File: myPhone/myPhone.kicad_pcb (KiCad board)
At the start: 2 copper layers, 135 x 70 mm, 211 parts, among them J1 USB_OTG, J2 BATT, J201 ESP32.UART, J202 Modem, J203 SIM_Card, J204 Motor, J205 Micro_SD_Card, J206 Camera, J207 GPS, J3 RV.Debug, J301 iMX8, J4 SJ-3571N, J5 Display, J6 Touch, Q1 MMBT3906, SW1 RESET, SW2 WAKE, SW201 BOOT, U1 BQ25895, U10 74HC595, U11 ICS-43434, U12 MAX98357A, U13 FT813Q, U14 FAN5333BSX, U2 TPS62293, U201 ESP32-WROOM, U202 SN74CBTLV3125, U203 TXB0104RGY, U204 TXB0104RGY, U205 DRV2605L, U206 SN74CBTLV3126, U207 TPS22917, U208 SN74LVC2G66, U209 TPS22917, U3 TPS630250, U4 SN74LVC2G07, U5 E310-G000, U6 IS25LP128-JBLE, U7 74HC00, U8 74HC00, U9 74HC595, X1 SiT1533, Y1 16MHz, Y2 12MHz

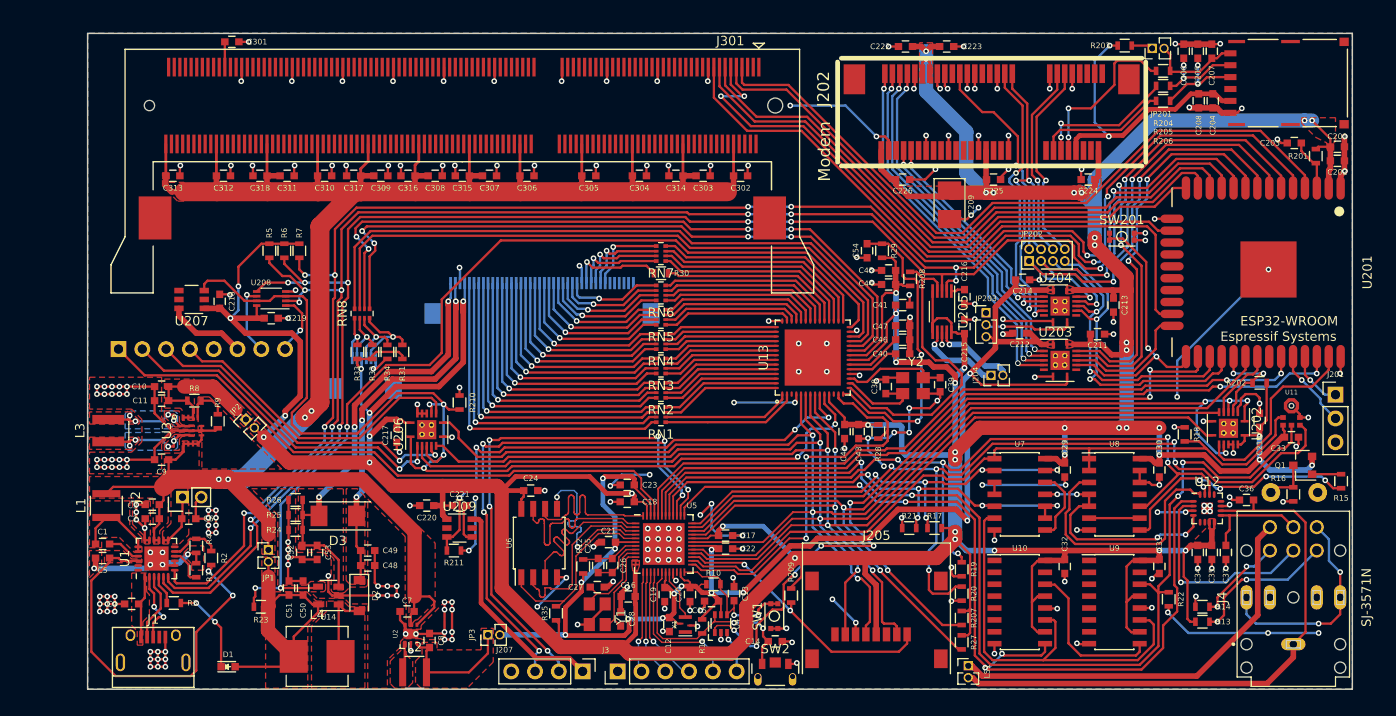
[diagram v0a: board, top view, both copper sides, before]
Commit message: upgrade to kicad 5; fixed footprints
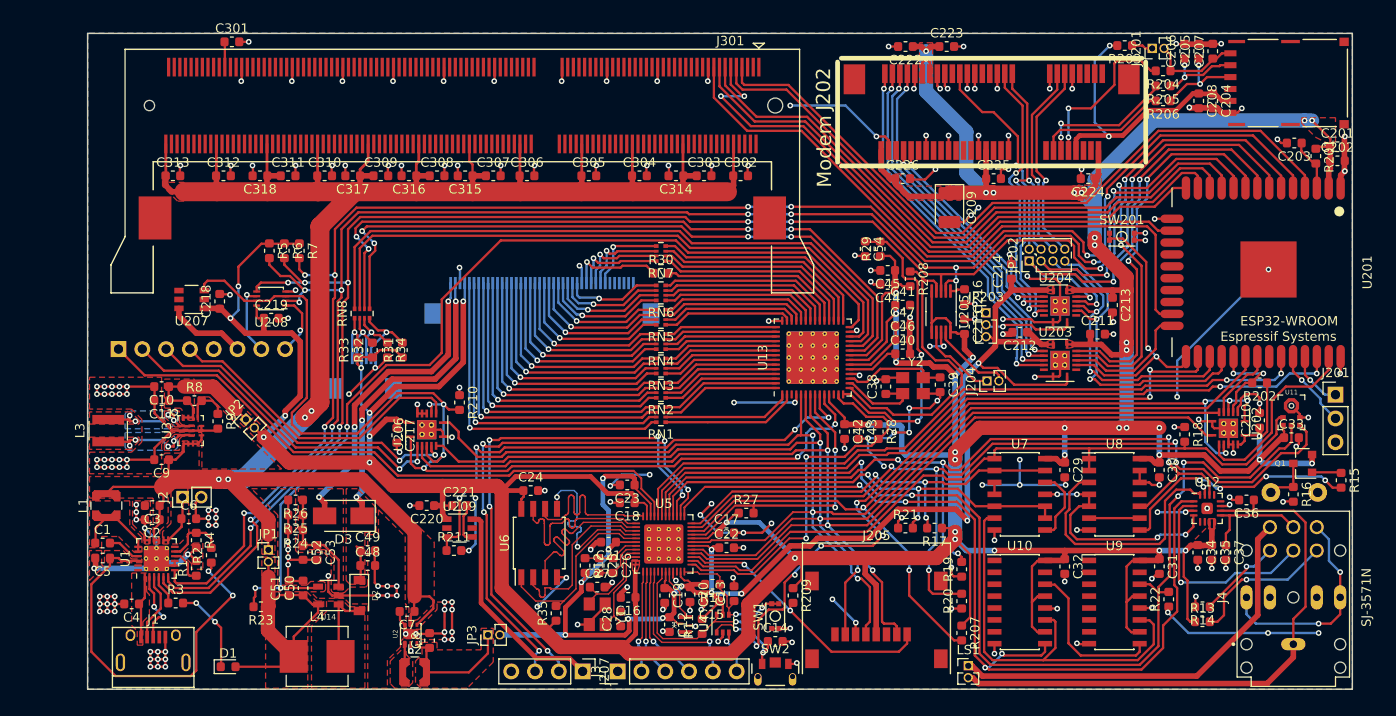
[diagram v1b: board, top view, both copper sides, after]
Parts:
- C1, C10, C11, C12, C13, C14, C15, C16, C17, C18, C19, C2, C20, C201, C202, C203, C204, C205, C206, C207, C208, C21, C210, C211, C212, C213, C214, C215, C216, C217, C218, C219, C22, C220, C221, C222, C223, C224, C225, C226, C23, C24, C25, C26, C27, C28, C29, C3, C30, C301, C302, C303, C304, C305, C306, C307, C308, C309, C31, C310, C311, C312, C313, C314, C315, C316, C317, C318, C32, C33, C34, C35, C36, C37, C38, C39, C4, C40, C41, C42, C43, C44, C45, C46, C47, C48, C49, C5, C50, C51, C52, C53, C54, C6, C7, C8, C9: footprint Capacitors_SMD:C_0603 -> Capacitor_SMD:C_0603_1608Metric
- C209: footprint Capacitors_Tantalum_SMD:CP_Tantalum_Case-B_EIA-3528-21_Reflow -> Capacitor_Tantalum_SMD:CP_EIA-3528-21_Kemet-B
- D1: footprint LEDs:LED_0603 -> LED_SMD:LED_0603_1608Metric
- D2: footprint Diodes_SMD:D_SOD-123 -> Diode_SMD:D_SOD-123
- D3: footprint footprints:DO-214AC -> Diode_SMD:D_SMA
- J2: footprint Pin_Headers:Pin_Header_Straight_1x02_Pitch2.00mm -> Connector_PinHeader_2.00mm:PinHeader_1x02_P2.00mm_Vertical
- J201: footprint Pin_Headers:Pin_Header_Straight_1x03_Pitch2.54mm -> Connector_PinHeader_2.54mm:PinHeader_1x03_P2.54mm_Vertical
- J204, JP1, JP2, JP201, JP3, LS1: footprint Pin_Headers:Pin_Header_Straight_1x02_Pitch1.27mm -> Connector_PinHeader_1.27mm:PinHeader_1x02_P1.27mm_Vertical
- J206: footprint Pin_Headers:Pin_Header_Straight_1x08_Pitch2.54mm -> Connector_PinHeader_2.54mm:PinHeader_1x08_P2.54mm_Vertical
- J207: footprint Pin_Headers:Pin_Header_Straight_1x04_Pitch2.54mm -> Connector_PinHeader_2.54mm:PinHeader_1x04_P2.54mm_Vertical
- J3: footprint Pin_Headers:Pin_Header_Straight_1x06_Pitch2.54mm -> Connector_PinHeader_2.54mm:PinHeader_1x06_P2.54mm_Vertical
- JP202: footprint Pin_Headers:Pin_Header_Straight_2x04_Pitch1.27mm -> Connector_PinHeader_1.27mm:PinHeader_2x04_P1.27mm_Vertical
- JP203: footprint Pin_Headers:Pin_Header_Straight_1x03_Pitch1.27mm -> Connector_PinHeader_1.27mm:PinHeader_1x03_P1.27mm_Vertical
- L1, L2: footprint footprints:Coilcraft_LPS3015 -> footprints:L_Coilcraft_LPS3015
- L3: footprint footprints:Coilcraft_XAL40 -> footprints:L_Coilcraft_XAL40
- L4: footprint footprints:Murata_LQH66SN -> footprints:L_Murata_LQH66SN
- Q1: footprint TO_SOT_Packages_SMD:SOT-23 -> Package_TO_SOT_SMD:SOT-23
- R1, R10, R11, R12, R13, R14, R15, R16, R17, R18, R19, R2, R20, R201, R202, R203, R204, R205, R206, R207, R208, R209, R21, R210, R211, R22, R23, R24, R25, R26, R27, R28, R29, R3, R30, R31, R32, R33, R34, R35, R4, R5, R6, R7, R8, R9: footprint Resistors_SMD:R_0603 -> Resistor_SMD:R_0603_1608Metric
- U1: footprint footprints:QFN-24-1EP_4x4mm_Pitch0.5mm -> Package_DFN_QFN:Texas_S-PWQFN-N24_EP2.7x2.7mm_ThermalVias
- U10, U9: footprint Housings_SOIC:SOIC-16_3.9x9.9mm_Pitch1.27mm -> Package_SO:SOIC-16_3.9x9.9mm_P1.27mm
- U12: footprint footprints:MAX98357 -> Package_DFN_QFN:TQFN-16-1EP_3x3mm_P0.5mm_EP1.23x1.23mm
- U13: footprint footprints:FT813Q -> Package_DFN_QFN:QFN-56-1EP_8x8mm_P0.5mm_EP5.6x5.6mm_ThermalVias
- U14: footprint TO_SOT_Packages_SMD:SOT-23-5 -> Package_TO_SOT_SMD:SOT-23-5
- U202, U203, U204, U206: footprint footprints:Texas_S-PVQFN-N14_ThermalVias -> Package_DFN_QFN:Texas_S-PVQFN-N14_ThermalVias
- U205: footprint footprints:VSSOP-10_3x3mm_Pitch0.5mm -> Package_SO:VSSOP-10_3x3mm_P0.5mm
- U208: footprint Housings_SSOP:VSSOP-8_2.3x2mm_Pitch0.5mm -> Package_SO:VSSOP-8_2.4x2.1mm_P0.5mm
- U4: footprint TO_SOT_Packages_SMD:SC-70-6 -> Package_TO_SOT_SMD:SOT-363_SC-70-6
- U5: footprint Housings_DFN_QFN:UQFN-48-1EP_6x6mm_Pitch0.4mm -> Package_DFN_QFN:QFN-48-1EP_6x6mm_P0.4mm_EP4.2x4.2mm_ThermalVias
- U6: footprint Housings_SOIC:SOIJ-8_5.3x5.3mm_Pitch1.27mm -> Package_SO:SOIJ-8_5.3x5.3mm_P1.27mm
- U7, U8: footprint Housings_SOIC:SOIC-14_3.9x8.7mm_Pitch1.27mm -> Package_SO:SOIC-14_3.9x8.7mm_P1.27mm
- moved R27 26.8 mm to (167.5, 123.0), turned to 0 degrees
- moved R207 1.60 mm to (190.5, 135.8)
- moved C214 1.50 mm to (195.8, 97.2), turned to 90 degrees
- moved R20 0.80 mm to (190.5, 132.4)
- moved J204 0.74 mm to (193.2, 108.9)
- moved D3 0.60 mm to (124.5, 123.3)
- moved R4 0.60 mm to (108.8, 125.9)
- moved C307 0.40 mm to (140.5, 87.0)
- moved R21 0.40 mm to (184.5, 124.6)
- moved C17 0.32 mm to (165.4, 125.1)
- moved C209 0.30 mm to (189.2, 90.4)
- moved C315 0.30 mm to (137.5, 87.0)
- moved R2 0.30 mm to (110.4, 127.5)
- moved C54 0.28 mm to (180.2, 94.8)
- moved R29 0.28 mm to (181.8, 94.8)
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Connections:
- J1 pad 4: Net-(J1-Pad4) -> (no net)
- J202 pad 1: Net-(J202-Pad1) -> (no net)
- J202 pad 16: Net-(J202-Pad16) -> (no net)
- J202 pad 20: Net-(J202-Pad20) -> (no net)
- J202 pad 22: Net-(J202-Pad22) -> (no net)
- J202 pad 23: Net-(J202-Pad23) -> (no net)
- J202 pad 25: Net-(J202-Pad25) -> (no net)
- J202 pad 28: Net-(J202-Pad28) -> (no net)
- J202 pad 3: Net-(J202-Pad3) -> (no net)
- J202 pad 30: Net-(J202-Pad30) -> (no net)
- J202 pad 32: Net-(J202-Pad32) -> (no net)
- J202 pad 33: Net-(J202-Pad33) -> (no net)
- J202 pad 36: Net-(J202-Pad36) -> (no net)
- J202 pad 38: Net-(J202-Pad38) -> (no net)
- J202 pad 42: Net-(J202-Pad42) -> (no net)
- J202 pad 48: Net-(J202-Pad48) -> (no net)
- J202 pad 5: Net-(J202-Pad5) -> (no net)
- J202 pad 6: Net-(J202-Pad6) -> (no net)
- J202 pad 7: Net-(J202-Pad7) -> (no net)
- J203 pad 6: Net-(J203-Pad6) -> (no net)
- J205 pad 3: Net-(J205-Pad3) -> (no net)
- J205 pad 8: Net-(J205-Pad8) -> (no net)
- J301 pad 100: Net-(J301-Pad100) -> (no net)
- J301 pad 101: Net-(J301-Pad101) -> (no net)
- J301 pad 102: Net-(J301-Pad102) -> (no net)
- J301 pad 103: Net-(J301-Pad103) -> (no net)
- J301 pad 104: Net-(J301-Pad104) -> (no net)
- J301 pad 106: Net-(J301-Pad106) -> (no net)
- J301 pad 107: Net-(J301-Pad107) -> (no net)
- J301 pad 108: Net-(J301-Pad108) -> (no net)
- J301 pad 109: Net-(J301-Pad109) -> (no net)
- J301 pad 110: Net-(J301-Pad110) -> (no net)
- J301 pad 111: Net-(J301-Pad111) -> (no net)
- J301 pad 112: Net-(J301-Pad112) -> (no net)
- J301 pad 113: Net-(J301-Pad113) -> (no net)
- J301 pad 115: Net-(J301-Pad115) -> (no net)
- J301 pad 116: Net-(J301-Pad116) -> (no net)
- J301 pad 117: Net-(J301-Pad117) -> (no net)
- J301 pad 118: Net-(J301-Pad118) -> (no net)
- J301 pad 119: Net-(J301-Pad119) -> (no net)
- J301 pad 12: Net-(J301-Pad12) -> (no net)
- J301 pad 120: Net-(J301-Pad120) -> (no net)
- J301 pad 121: Net-(J301-Pad121) -> (no net)
- J301 pad 122: Net-(J301-Pad122) -> (no net)
- J301 pad 124: Net-(J301-Pad124) -> (no net)
- J301 pad 125: Net-(J301-Pad125) -> (no net)
- J301 pad 126: Net-(J301-Pad126) -> (no net)
- J301 pad 127: Net-(J301-Pad127) -> (no net)
- J301 pad 128: Net-(J301-Pad128) -> (no net)
- J301 pad 129: Net-(J301-Pad129) -> (no net)
- J301 pad 130: Net-(J301-Pad130) -> (no net)
- J301 pad 131: Net-(J301-Pad131) -> (no net)
- J301 pad 133: Net-(J301-Pad133) -> (no net)
- J301 pad 134: Net-(J301-Pad134) -> (no net)
- J301 pad 135: Net-(J301-Pad135) -> (no net)
- J301 pad 136: Net-(J301-Pad136) -> (no net)
- J301 pad 137: Net-(J301-Pad137) -> (no net)
- J301 pad 138: Net-(J301-Pad138) -> (no net)
- J301 pad 139: Net-(J301-Pad139) -> (no net)
- J301 pad 14: Net-(J301-Pad14) -> (no net)
- J301 pad 140: Net-(J301-Pad140) -> (no net)
- J301 pad 142: Net-(J301-Pad142) -> (no net)
- J301 pad 143: Net-(J301-Pad143) -> (no net)
- J301 pad 144: Net-(J301-Pad144) -> (no net)
- J301 pad 145: Net-(J301-Pad145) -> (no net)
- J301 pad 146: Net-(J301-Pad146) -> (no net)
- J301 pad 147: Net-(J301-Pad147) -> (no net)
- J301 pad 148: Net-(J301-Pad148) -> (no net)
- J301 pad 149: Net-(J301-Pad149) -> (no net)
- J301 pad 151: Net-(J301-Pad151) -> (no net)
- J301 pad 152: Net-(J301-Pad152) -> (no net)
- J301 pad 153: Net-(J301-Pad153) -> (no net)
- J301 pad 154: Net-(J301-Pad154) -> (no net)
- J301 pad 155: Net-(J301-Pad155) -> (no net)
- J301 pad 156: Net-(J301-Pad156) -> (no net)
- J301 pad 157: Net-(J301-Pad157) -> (no net)
- J301 pad 158: Net-(J301-Pad158) -> (no net)
- J301 pad 16: Net-(J301-Pad16) -> (no net)
- J301 pad 160: Net-(J301-Pad160) -> (no net)
- J301 pad 161: Net-(J301-Pad161) -> (no net)
- J301 pad 162: Net-(J301-Pad162) -> (no net)
- J301 pad 163: Net-(J301-Pad163) -> (no net)
- J301 pad 164: Net-(J301-Pad164) -> (no net)
- J301 pad 165: Net-(J301-Pad165) -> (no net)
- J301 pad 166: Net-(J301-Pad166) -> (no net)
- J301 pad 167: Net-(J301-Pad167) -> (no net)
- J301 pad 169: Net-(J301-Pad169) -> (no net)
- J301 pad 170: Net-(J301-Pad170) -> (no net)
- J301 pad 171: Net-(J301-Pad171) -> (no net)
- J301 pad 172: Net-(J301-Pad172) -> (no net)
- J301 pad 173: Net-(J301-Pad173) -> (no net)
- J301 pad 174: Net-(J301-Pad174) -> (no net)
- J301 pad 175: Net-(J301-Pad175) -> (no net)
- J301 pad 176: Net-(J301-Pad176) -> (no net)
- J301 pad 178: Net-(J301-Pad178) -> (no net)
- J301 pad 179: Net-(J301-Pad179) -> (no net)
- J301 pad 18: Net-(J301-Pad18) -> (no net)
- J301 pad 180: Net-(J301-Pad180) -> (no net)
- J301 pad 181: Net-(J301-Pad181) -> (no net)
- J301 pad 182: Net-(J301-Pad182) -> (no net)
- J301 pad 184: Net-(J301-Pad184) -> (no net)
- J301 pad 185: Net-(J301-Pad185) -> (no net)
- J301 pad 187: Net-(J301-Pad187) -> (no net)
- J301 pad 188: Net-(J301-Pad188) -> (no net)
- J301 pad 189: Net-(J301-Pad189) -> (no net)
- J301 pad 190: Net-(J301-Pad190) -> (no net)
- J301 pad 191: Net-(J301-Pad191) -> (no net)
- J301 pad 192: Net-(J301-Pad192) -> (no net)
- J301 pad 193: Net-(J301-Pad193) -> (no net)
- J301 pad 194: Net-(J301-Pad194) -> (no net)
- J301 pad 195: Net-(J301-Pad195) -> (no net)
- J301 pad 196: Net-(J301-Pad196) -> (no net)
- J301 pad 197: Net-(J301-Pad197) -> (no net)
- J301 pad 198: Net-(J301-Pad198) -> (no net)
- J301 pad 199: Net-(J301-Pad199) -> (no net)
- J301 pad 2: Net-(J301-Pad2) -> (no net)
- J301 pad 20: Net-(J301-Pad20) -> (no net)
- J301 pad 200: Net-(J301-Pad200) -> (no net)
- J301 pad 201: Net-(J301-Pad201) -> (no net)
- J301 pad 202: Net-(J301-Pad202) -> (no net)
- J301 pad 203: Net-(J301-Pad203) -> (no net)
- J301 pad 21: Net-(J301-Pad21) -> (no net)
- J301 pad 22: Net-(J301-Pad22) -> (no net)
- J301 pad 23: Net-(J301-Pad23) -> (no net)
- J301 pad 24: Net-(J301-Pad24) -> (no net)
- J301 pad 25: Net-(J301-Pad25) -> (no net)
- J301 pad 26: Net-(J301-Pad26) -> (no net)
- J301 pad 27: Net-(J301-Pad27) -> (no net)
- J301 pad 29: Net-(J301-Pad29) -> (no net)
- J301 pad 3: Net-(J301-Pad3) -> (no net)
- J301 pad 30: Net-(J301-Pad30) -> (no net)
- J301 pad 31: Net-(J301-Pad31) -> (no net)
- J301 pad 32: Net-(J301-Pad32) -> (no net)
- J301 pad 33: Net-(J301-Pad33) -> (no net)
- J301 pad 34: Net-(J301-Pad34) -> (no net)
- J301 pad 35: Net-(J301-Pad35) -> (no net)
- J301 pad 36: Net-(J301-Pad36) -> (no net)
- J301 pad 38: Net-(J301-Pad38) -> (no net)
- J301 pad 39: Net-(J301-Pad39) -> (no net)
- J301 pad 4: Net-(J301-Pad4) -> (no net)
- J301 pad 40: Net-(J301-Pad40) -> (no net)
- J301 pad 41: Net-(J301-Pad41) -> (no net)
- J301 pad 42: Net-(J301-Pad42) -> (no net)
- J301 pad 43: Net-(J301-Pad43) -> (no net)
- J301 pad 44: Net-(J301-Pad44) -> (no net)
- J301 pad 45: Net-(J301-Pad45) -> (no net)
- J301 pad 47: Net-(J301-Pad47) -> (no net)
- J301 pad 48: Net-(J301-Pad48) -> (no net)
- J301 pad 49: Net-(J301-Pad49) -> (no net)
- J301 pad 5: Net-(J301-Pad5) -> (no net)
- J301 pad 50: Net-(J301-Pad50) -> (no net)
- J301 pad 51: Net-(J301-Pad51) -> (no net)
- J301 pad 52: Net-(J301-Pad52) -> (no net)
- J301 pad 53: Net-(J301-Pad53) -> (no net)
- J301 pad 54: Net-(J301-Pad54) -> (no net)
- J301 pad 56: Net-(J301-Pad56) -> (no net)
- J301 pad 57: Net-(J301-Pad57) -> (no net)
- J301 pad 58: Net-(J301-Pad58) -> (no net)
- J301 pad 59: Net-(J301-Pad59) -> (no net)
- J301 pad 6: Net-(J301-Pad6) -> (no net)
- J301 pad 60: Net-(J301-Pad60) -> (no net)
- J301 pad 61: Net-(J301-Pad61) -> (no net)
- J301 pad 62: Net-(J301-Pad62) -> (no net)
- J301 pad 63: Net-(J301-Pad63) -> (no net)
- J301 pad 65: Net-(J301-Pad65) -> (no net)
- J301 pad 66: Net-(J301-Pad66) -> (no net)
- J301 pad 67: Net-(J301-Pad67) -> (no net)
- J301 pad 68: Net-(J301-Pad68) -> (no net)
- J301 pad 69: Net-(J301-Pad69) -> (no net)
- J301 pad 70: Net-(J301-Pad70) -> (no net)
- J301 pad 72: Net-(J301-Pad72) -> (no net)
- J301 pad 73: Net-(J301-Pad73) -> (no net)
- J301 pad 74: Net-(J301-Pad74) -> (no net)
- J301 pad 75: Net-(J301-Pad75) -> (no net)
- J301 pad 76: Net-(J301-Pad76) -> (no net)
- J301 pad 77: Net-(J301-Pad77) -> (no net)
- J301 pad 79: Net-(J301-Pad79) -> (no net)
- J301 pad 8: Net-(J301-Pad8) -> (no net)
- J301 pad 80: Net-(J301-Pad80) -> (no net)
- J301 pad 81: Net-(J301-Pad81) -> (no net)
- J301 pad 82: Net-(J301-Pad82) -> (no net)
- J301 pad 83: Net-(J301-Pad83) -> (no net)
- J301 pad 84: Net-(J301-Pad84) -> (no net)
- J301 pad 85: Net-(J301-Pad85) -> (no net)
- J301 pad 86: Net-(J301-Pad86) -> (no net)
- J301 pad 88: Net-(J301-Pad88) -> (no net)
- J301 pad 89: Net-(J301-Pad89) -> (no net)
- J301 pad 90: Net-(J301-Pad90) -> (no net)
- J301 pad 91: Net-(J301-Pad91) -> (no net)
- J301 pad 92: Net-(J301-Pad92) -> (no net)
- J301 pad 93: Net-(J301-Pad93) -> (no net)
- J301 pad 94: Net-(J301-Pad94) -> (no net)
- J301 pad 95: Net-(J301-Pad95) -> (no net)
- J301 pad 97: Net-(J301-Pad97) -> (no net)
- J301 pad 98: Net-(J301-Pad98) -> (no net)
- J301 pad 99: Net-(J301-Pad99) -> (no net)
- J4 pad 10: Net-(J4-Pad10) -> (no net)
- J4 pad 11: Net-(J4-Pad11) -> (no net)
- J5 pad 35: Net-(J5-Pad35) -> (no net)
- J5 pad 37: Net-(J5-Pad37) -> (no net)
- J5 pad 38: Net-(J5-Pad38) -> (no net)
- J5 pad 39: Net-(J5-Pad39) -> (no net)
- J5 pad 40: Net-(J5-Pad40) -> (no net)
- U1 pad 12: Net-(U1-Pad12) -> (no net)
- U1 pad 23: Net-(U1-Pad23) -> (no net)
- U1 pad 24: Net-(U1-Pad24) -> (no net)
- U10 pad 1: Net-(U10-Pad1) -> (no net)
- U10 pad 15: Net-(U10-Pad15) -> (no net)
- U10 pad 2: Net-(U10-Pad2) -> (no net)
- U10 pad 3: Net-(U10-Pad3) -> (no net)
- U10 pad 4: Net-(U10-Pad4) -> (no net)
- U10 pad 5: Net-(U10-Pad5) -> (no net)
- U10 pad 6: Net-(U10-Pad6) -> (no net)
- U10 pad 7: Net-(U10-Pad7) -> (no net)
- U13 pad 12: Net-(U13-Pad12) -> (no net)
- U13 pad 3: Net-(U13-Pad3) -> (no net)
- U201 pad 17: Net-(U201-Pad17) -> (no net)
- U201 pad 18: Net-(U201-Pad18) -> (no net)
- U201 pad 19: Net-(U201-Pad19) -> (no net)
- U201 pad 20: Net-(U201-Pad20) -> (no net)
- U201 pad 21: Net-(U201-Pad21) -> (no net)
- U201 pad 22: Net-(U201-Pad22) -> (no net)
- U201 pad 32: Net-(U201-Pad32) -> (no net)
- U203 pad 6: Net-(U203-Pad6) -> (no net)
- U203 pad 9: Net-(U203-Pad9) -> (no net)
- U204 pad 6: Net-(U204-Pad6) -> (no net)
- U204 pad 9: Net-(U204-Pad9) -> (no net)
- U207 pad 4: Net-(U207-Pad4) -> (no net)
- U207 pad 5: Net-(U207-Pad5) -> (no net)
- U209 pad 5: Net-(U209-Pad5) -> (no net)
- U5 pad 17: Net-(U5-Pad17) -> (no net)
- U5 pad 22: Net-(U5-Pad22) -> (no net)
- U8 pad 11: Net-(U8-Pad11) -> (no net)
- U9 pad 1: Net-(U9-Pad1) -> (no net)
- U9 pad 15: Net-(U9-Pad15) -> (no net)
- U9 pad 2: Net-(U9-Pad2) -> (no net)
- U9 pad 3: Net-(U9-Pad3) -> (no net)
- U9 pad 4: Net-(U9-Pad4) -> (no net)
- U9 pad 5: Net-(U9-Pad5) -> (no net)
- U9 pad 6: Net-(U9-Pad6) -> (no net)
- U9 pad 7: Net-(U9-Pad7) -> (no net)
- X1 pad 1: Net-(X1-Pad1) -> (no net)
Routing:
- net GND: track 458.6 -> 489.1 mm, vias 264 -> 240
- net SPI1.SS2: track 50.7 -> 30.6 mm, vias 3 -> 2
- net +3V3: track 674.0 -> 668.5 mm, vias 46 -> 45
- net PWM2.2: track 50.1 -> 46.1 mm, vias 5 -> 3
- net /DISP_LED_A: track 39.9 -> 36.1 mm
- net GPIO_18: track 53.8 -> 50.0 mm, vias 5 -> 3
- net GPIO_0: track 42.4 -> 40.4 mm
- net PWM0.1: track 78.4 -> 76.5 mm
- net /DISP_LED_K: track 47.9 -> 46.0 mm
- net +1V8: track 180.3 -> 179.0 mm
- net Net-(C13-Pad1): track 16.4 -> 15.3 mm
- net Net-(R2-Pad2): track 5.50 -> 6.58 mm
- net FT813.GPIO3: track 33.7 -> 32.6 mm
- net Net-(J6-Pad5): track 8.99 -> 8.25 mm
- net SPI1.SS3: track 97.1 -> 96.4 mm
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
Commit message: REV1 board
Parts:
- removed C15: 0.1uF, Capacitor_SMD:C_0603_1608Metric
- removed C209: 470uF, Capacitor_Tantalum_SMD:CP_EIA-3528-21_Kemet-B
- removed J201: ESP32.UART, Connector_PinHeader_2.54mm:PinHeader_1x03_P2.54mm_Vertical
- removed J207: GPS, Connector_PinHeader_2.54mm:PinHeader_1x04_P2.54mm_Vertical
- removed J4: SJ-3571N, footprints:CUI_SJ-3571N
- removed J5: Display, footprints:Hirose_FH12-40S-0.5SH_1x40-1MP_P0.50mm_Horizontal_Bottom
- removed J6: Touch, footprints:Hirose_FH12-6S-0.5SH_1x06-1MP_P0.50mm_Horizontal_Bottom
- removed the JP202 at (197.7, 96.1)
- removed R30: 33R, Resistor_SMD:R_0603_1608Metric
- removed RN1, RN2, RN3, RN4, RN5, RN6, RN7, RN8: 33R, footprints:R_Array_Convex_4x0402
- removed U4: SN74LVC2G07, Package_TO_SOT_SMD:SOT-363_SC-70-6
- added C227: 470uF, Capacitor_Tantalum_SMD:CP_EIA-3528-21_Kemet-B, F.Cu at (190.1, 73.5)
- added C228: 470uF, Capacitor_Tantalum_SMD:CP_EIA-3528-21_Kemet-B, F.Cu at (183.3, 73.5)
- added C319: 1uF, Capacitor_SMD:C_0603_1608Metric, F.Cu at (127.6, 89.8)
- added C320: 0.1uF, Capacitor_SMD:C_0603_1608Metric, F.Cu at (129.1, 89.8)
- added C321: 1uF, Capacitor_SMD:C_0603_1608Metric, F.Cu at (127.6, 100.2)
- added C322: 0.1uF, Capacitor_SMD:C_0603_1608Metric, F.Cu at (129.1, 100.2)
- added C323: 0.1uF, Capacitor_SMD:C_0603_1608Metric, B.Cu at (147.9, 90.7)
- added C324: 0.01uF, Capacitor_SMD:C_0603_1608Metric, B.Cu at (147.9, 89.2)
- added C325: 1uF, Capacitor_SMD:C_0603_1608Metric, F.Cu at (137.9, 111.2)
- added C326: 0.1uF, Capacitor_SMD:C_0603_1608Metric, F.Cu at (137.9, 109.8)
- added C327: 1uF, Capacitor_SMD:C_0603_1608Metric, F.Cu at (148.3, 111.2)
- added C328: 0.1uF, Capacitor_SMD:C_0603_1608Metric, F.Cu at (148.3, 109.8)
- added C329: 0.1uF, Capacitor_SMD:C_0603_1608Metric, B.Cu at (139.8, 94.5)
- added C330: 0.01uF, Capacitor_SMD:C_0603_1608Metric, B.Cu at (139.8, 93.0)
- added C331: 0.1uF, Capacitor_SMD:C_0603_1608Metric, B.Cu at (142.7, 95.0)
- added C332: 0.01uF, Capacitor_SMD:C_0603_1608Metric, B.Cu at (144.7, 95.0)
- added C333: 0.1uF, Capacitor_SMD:C_0603_1608Metric, B.Cu at (147.9, 94.2)
- added C334: 0.01uF, Capacitor_SMD:C_0603_1608Metric, B.Cu at (147.9, 92.7)
- added C335: 0.1uF, Capacitor_SMD:C_0603_1608Metric, B.Cu at (139.8, 88.8)
- added C336: 0.01uF, Capacitor_SMD:C_0603_1608Metric, B.Cu at (139.8, 90.2)
- added C337: 1uF, Capacitor_SMD:C_0603_1608Metric, F.Cu at (151.3, 111.2)
- added C338: 0.1uF, Capacitor_SMD:C_0603_1608Metric, F.Cu at (151.3, 109.8)
- added C339: 1uF, Capacitor_SMD:C_0603_1608Metric, F.Cu at (161.7, 111.2)
- added C340: 0.1uF, Capacitor_SMD:C_0603_1608Metric, F.Cu at (161.7, 109.8)
- added C341: 0.1uF, Capacitor_SMD:C_0603_1608Metric, F.Cu at (127.2, 107.2)
- added C342: 0.1uF, Capacitor_SMD:C_0603_1608Metric, F.Cu at (136.7, 115.2)
- added J302: Touch, Connector_FFC-FPC:Hirose_FH12-6S-0.5SH_1x06-1MP_P0.50mm_Horizontal, B.Cu at (126.7, 105.3)
- added J303: Display, Connector_FFC-FPC:Hirose_FH12-40S-0.5SH_1x40-1MP_P0.50mm_Horizontal, B.Cu at (145.7, 113.3)
- added J304: Prog, Connector_FFC-FPC:Hirose_FH12-12S-0.5SH_1x12-1MP_P0.50mm_Horizontal, B.Cu at (141.3, 136.9)
- added JP203: Q.DTR, Connector_PinHeader_1.27mm:PinHeader_1x02_P1.27mm_Vertical, F.Cu at (195.1, 73.4)
- added JP204: Q.RI, Connector_PinHeader_1.27mm:PinHeader_1x02_P1.27mm_Vertical, F.Cu at (198.7, 73.4)
- added JP205: Q.TXD, Connector_PinHeader_1.27mm:PinHeader_1x02_P1.27mm_Vertical, F.Cu at (202.2, 73.4)
- added JP206: Q.RXD, Connector_PinHeader_1.27mm:PinHeader_1x02_P1.27mm_Vertical, F.Cu at (205.8, 73.4)
- added R36: 100K, Resistor_SMD:R_0603_1608Metric, F.Cu at (138.0, 133.3)
- added U301: SN65LVDS822_SWAP, Package_DFN_QFN:QFN-48-1EP_7x7mm_P0.5mm_EP5.15x5.15mm_ThermalVias, F.Cu at (143.8, 90.9)
- added U302: TS3DDR3812, footprints:Texas_R-PWQFN-N42, F.Cu at (132.8, 95.0)
- added U303: TS3DDR3812, footprints:Texas_R-PWQFN-N42, F.Cu at (143.1, 106.0)
- added U304: TS3DDR3812, footprints:Texas_R-PWQFN-N42, F.Cu at (156.5, 106.0)
- C222, C223, C224, C225, C226, C301, C302, C303, C304, C305, C306, C307, C308, C309, C310, C311, C312, C313, C314, C315, C316, C317, C318, J203, J205: moved to B.Cu
- J3: value RV.Debug -> SJ-3571N; footprint Connector_PinHeader_2.54mm:PinHeader_1x06_P2.54mm_Vertical -> footprints:CUI_SJ-3571N
- R208: value 47K -> 100K
- U10, U9: footprint Package_SO:SOIC-16_3.9x9.9mm_P1.27mm -> footprints:74HC595BQ115
- U12: footprint Package_DFN_QFN:TQFN-16-1EP_3x3mm_P0.5mm_EP1.23x1.23mm -> footprints:TQFN-16-1EP_3x3mm_P0.5mm_EP1.23x1.23mm_ThermalVias
- U5: value E310-G000 -> E310-G002
- U7, U8: footprint Package_SO:SOIC-14_3.9x8.7mm_P1.27mm -> footprints:74HC00BQ115
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- renumbered C20 to C19, C22 to C20, C23 to C21, C19 to C22, C21 to C23, JP203 to JP202, R31 to R301, R32 to R302, R33 to R303, R34 to R304
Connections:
- net /DISP_LED_A renamed DISP_LED_A
- net /DISP_LED_K renamed DISP_LED_K
- net Net-(C25-Pad2) renamed /PLL_AVSS
- net Net-(C27-Pad1) renamed /XTAL_XI
- net Net-(C28-Pad1) renamed /XTAL_XO
- net Net-(R35-Pad2) renamed /QSPI_CS
- net Net-(U5-Pad1) renamed /QSPI_DQ_3
- net Net-(U5-Pad2) renamed /QSPI_DQ_2
- net Net-(U5-Pad20) renamed /PSD_LFALTCLK
- net Net-(U5-Pad3) renamed /QSPI_DQ_1
- net Net-(U5-Pad4) renamed /QSPI_DQ_0
- net Net-(U5-Pad48) renamed /QSPI_CLK
- C12 pad 1: +1V8 -> +3V3
- C13 pad 1: Net-(C13-Pad1) -> RESET
- C14 pad 1: Net-(C14-Pad1) -> WAKE
- C19 pad 1: +1V8 -> +3V3
- C23 pad 1: +1V8 -> +3V3
- C25 pad 1: Net-(C25-Pad1) -> /PLL_AVDD
- C26 pad 1: Net-(C25-Pad1) -> /PLL_AVDD
- J1 pad 4: (no net) -> Net-(J1-Pad4)
- J202 pad 1: (no net) -> Net-(J202-Pad1)
- J202 pad 16: (no net) -> Net-(J202-Pad16)
- J202 pad 20: (no net) -> Net-(J202-Pad20)
- J202 pad 22: (no net) -> Net-(J202-Pad22)
- J202 pad 23: (no net) -> Net-(J202-Pad23)
- J202 pad 25: (no net) -> Net-(J202-Pad25)
- J202 pad 28: (no net) -> Net-(J202-Pad28)
- J202 pad 3: (no net) -> Net-(J202-Pad3)
- J202 pad 30: (no net) -> Net-(J202-Pad30)
- J202 pad 32: (no net) -> Net-(J202-Pad32)
- J202 pad 33: (no net) -> Net-(J202-Pad33)
- J202 pad 36: (no net) -> iMX8_USB1_D_N
- J202 pad 38: (no net) -> iMX8_USB1_D_P
- J202 pad 42: (no net) -> Net-(J202-Pad42)
- J202 pad 48: (no net) -> Net-(J202-Pad48)
- J202 pad 5: (no net) -> Net-(J202-Pad5)
- J202 pad 6: (no net) -> Net-(J202-Pad6)
- J202 pad 7: (no net) -> Net-(J202-Pad7)
- J203 pad 6: (no net) -> Net-(J203-Pad6)
- J205 pad 3: (no net) -> Net-(J205-Pad3)
- J205 pad 8: (no net) -> Net-(J205-Pad8)
- J3 pad 1: GND -> /SPK_VO-
- J3 pad 2: JTAG_TCK -> Net-(J3-Pad2)
- J3 pad 3: JTAG_TDO -> Net-(J3-Pad2)
- J3 pad 4: JTAG_TMS -> Net-(J3-Pad4)
- J3 pad 5: JTAG_TDI -> /SPK_GAIN
- J3 pad 6: RESET -> Net-(J3-Pad6)
- J301 pad 100: (no net) -> Net-(J301-Pad100)
- J301 pad 101: (no net) -> Net-(J301-Pad101)
- J301 pad 102: (no net) -> Net-(J301-Pad102)
- J301 pad 103: (no net) -> Net-(J301-Pad103)
- J301 pad 104: (no net) -> Net-(J301-Pad104)
- J301 pad 106: (no net) -> Net-(J301-Pad106)
- J301 pad 107: (no net) -> Net-(J301-Pad107)
- J301 pad 108: (no net) -> Net-(J301-Pad108)
- J301 pad 109: (no net) -> Net-(J301-Pad109)
- J301 pad 110: (no net) -> Net-(J301-Pad110)
- J301 pad 111: (no net) -> Net-(J301-Pad111)
- J301 pad 112: (no net) -> Net-(J301-Pad112)
- J301 pad 113: (no net) -> Net-(J301-Pad113)
- J301 pad 115: (no net) -> Net-(J301-Pad115)
- J301 pad 116: (no net) -> Net-(J301-Pad116)
- J301 pad 117: (no net) -> Net-(J301-Pad117)
- J301 pad 118: (no net) -> Net-(J301-Pad118)
- J301 pad 119: (no net) -> Net-(J301-Pad119)
- J301 pad 12: (no net) -> Net-(J301-Pad12)
- J301 pad 120: (no net) -> Net-(J301-Pad120)
- J301 pad 121: (no net) -> Net-(J301-Pad121)
- J301 pad 122: (no net) -> Net-(J301-Pad122)
- J301 pad 124: (no net) -> Net-(J301-Pad124)
- J301 pad 125: (no net) -> Net-(J301-Pad125)
- J301 pad 126: (no net) -> Net-(J301-Pad126)
- J301 pad 127: (no net) -> Net-(J301-Pad127)
- J301 pad 128: (no net) -> Net-(J301-Pad128)
- J301 pad 129: (no net) -> iMX8_I2C1_SCL
- J301 pad 130: (no net) -> Net-(J301-Pad130)
- J301 pad 131: (no net) -> Net-(J301-Pad131)
- J301 pad 133: (no net) -> Net-(J301-Pad133)
- J301 pad 134: (no net) -> Net-(J301-Pad134)
- J301 pad 135: (no net) -> iMX8_I2C1_SDA
- J301 pad 136: (no net) -> Net-(J301-Pad136)
- J301 pad 137: (no net) -> Net-(J301-Pad137)
- J301 pad 138: (no net) -> Net-(J301-Pad138)
- J301 pad 139: (no net) -> Net-(J301-Pad139)
- J301 pad 14: (no net) -> Net-(J301-Pad14)
- J301 pad 140: (no net) -> Net-(J301-Pad140)
- J301 pad 142: (no net) -> Net-(J301-Pad142)
- J301 pad 143: (no net) -> Net-(J301-Pad143)
- J301 pad 144: (no net) -> Net-(J301-Pad144)
- J301 pad 145: (no net) -> Net-(J301-Pad145)
- J301 pad 146: (no net) -> Net-(J301-Pad146)
- J301 pad 147: (no net) -> Net-(J301-Pad147)
- J301 pad 148: (no net) -> Net-(J301-Pad148)
- J301 pad 149: (no net) -> iMX8_GPIO3_IO13
- J301 pad 151: (no net) -> iMX8_GPIO3_IO12
- J301 pad 152: (no net) -> Net-(J301-Pad152)
- J301 pad 153: (no net) -> iMX8_GPIO3_IO11
- J301 pad 154: (no net) -> Net-(J301-Pad154)
- J301 pad 155: (no net) -> Net-(J301-Pad155)
- J301 pad 156: (no net) -> Net-(J301-Pad156)
- J301 pad 157: (no net) -> Net-(J301-Pad157)
- J301 pad 158: (no net) -> Net-(J301-Pad158)
- J301 pad 16: (no net) -> Net-(J301-Pad16)
- J301 pad 160: (no net) -> Net-(J301-Pad160)
- J301 pad 161: (no net) -> Net-(J301-Pad161)
- J301 pad 162: (no net) -> Net-(J301-Pad162)
- J301 pad 163: (no net) -> Net-(J301-Pad163)
- J301 pad 164: (no net) -> Net-(J301-Pad164)
- J301 pad 165: (no net) -> Net-(J301-Pad165)
- J301 pad 166: (no net) -> Net-(J301-Pad166)
- J301 pad 167: (no net) -> Net-(J301-Pad167)
- J301 pad 169: (no net) -> Net-(J301-Pad169)
- J301 pad 170: (no net) -> Net-(J301-Pad170)
- J301 pad 171: (no net) -> Net-(J301-Pad171)
- J301 pad 172: (no net) -> Net-(J301-Pad172)
- J301 pad 173: (no net) -> Net-(J301-Pad173)
- J301 pad 174: (no net) -> Net-(J301-Pad174)
- J301 pad 175: (no net) -> Net-(J301-Pad175)
- J301 pad 176: (no net) -> iMX8_USB1_D_P
- J301 pad 178: (no net) -> iMX8_USB1_D_N
- J301 pad 179: (no net) -> Net-(J301-Pad179)
- J301 pad 18: (no net) -> Net-(J301-Pad18)
- J301 pad 180: (no net) -> Net-(J301-Pad180)
- J301 pad 181: (no net) -> Net-(J301-Pad181)
- J301 pad 182: (no net) -> Net-(J301-Pad182)
- J301 pad 184: (no net) -> Net-(J301-Pad184)
- J301 pad 185: (no net) -> Net-(J301-Pad185)
- J301 pad 187: (no net) -> Net-(J301-Pad187)
- J301 pad 188: (no net) -> Net-(J301-Pad188)
- J301 pad 189: (no net) -> Net-(J301-Pad189)
- J301 pad 190: (no net) -> Net-(J301-Pad190)
- J301 pad 191: (no net) -> Net-(J301-Pad191)
- J301 pad 192: (no net) -> Net-(J301-Pad192)
- J301 pad 193: (no net) -> Net-(J301-Pad193)
- J301 pad 194: (no net) -> Net-(J301-Pad194)
- J301 pad 195: (no net) -> Net-(J301-Pad195)
- J301 pad 196: (no net) -> Net-(J301-Pad196)
- J301 pad 197: (no net) -> Net-(J301-Pad197)
- J301 pad 198: (no net) -> Net-(J301-Pad198)
- J301 pad 199: (no net) -> Net-(J301-Pad199)
- J301 pad 2: (no net) -> Net-(J301-Pad2)
- J301 pad 20: (no net) -> Net-(J301-Pad20)
- J301 pad 200: (no net) -> Net-(J301-Pad200)
- J301 pad 201: (no net) -> Net-(J301-Pad201)
- J301 pad 202: (no net) -> Net-(J301-Pad202)
- J301 pad 203: (no net) -> Net-(J301-Pad203)
- J301 pad 21: (no net) -> Net-(J301-Pad21)
- J301 pad 22: (no net) -> Net-(J301-Pad22)
- J301 pad 23: (no net) -> Net-(J301-Pad23)
- J301 pad 24: (no net) -> Net-(J301-Pad24)
- J301 pad 25: (no net) -> Net-(J301-Pad25)
- J301 pad 26: (no net) -> Net-(J301-Pad26)
- J301 pad 27: (no net) -> Net-(J301-Pad27)
- J301 pad 29: (no net) -> Net-(J301-Pad29)
- J301 pad 3: (no net) -> Net-(J301-Pad3)
- J301 pad 30: (no net) -> Net-(J301-Pad30)
- J301 pad 31: (no net) -> Net-(J301-Pad31)
- J301 pad 32: (no net) -> Net-(J301-Pad32)
- J301 pad 33: (no net) -> iMX8_LVDS0_CLK_P
- J301 pad 34: (no net) -> Net-(J301-Pad34)
- J301 pad 35: (no net) -> iMX8_LVDS0_CLK_N
- J301 pad 36: (no net) -> Net-(J301-Pad36)
- J301 pad 38: (no net) -> Net-(J301-Pad38)
- J301 pad 39: (no net) -> iMX8_LVDS0_A0_P
- J301 pad 4: (no net) -> Net-(J301-Pad4)
- J301 pad 40: (no net) -> Net-(J301-Pad40)
- J301 pad 41: (no net) -> iMX8_LVDS0_A0_N
- J301 pad 42: (no net) -> Net-(J301-Pad42)
- J301 pad 43: (no net) -> Net-(J301-Pad43)
- J301 pad 44: (no net) -> Net-(J301-Pad44)
- J301 pad 45: (no net) -> iMX8_LVDS0_A1_P
- J301 pad 47: (no net) -> iMX8_LVDS0_A1_N
- J301 pad 48: (no net) -> Net-(J301-Pad48)
- J301 pad 49: (no net) -> Net-(J301-Pad49)
- J301 pad 5: (no net) -> iMX8_GPIO5_IO28
- J301 pad 50: (no net) -> Net-(J301-Pad50)
- J301 pad 51: (no net) -> iMX8_LVDS0_A2_P
- J301 pad 52: (no net) -> Net-(J301-Pad52)
- J301 pad 53: (no net) -> iMX8_LVDS0_A2_N
- J301 pad 54: (no net) -> Net-(J301-Pad54)
- J301 pad 56: (no net) -> Net-(J301-Pad56)
- J301 pad 57: (no net) -> iMX8_LVDS0_A3_P
- J301 pad 58: (no net) -> iMX8_GPIO5_IO25
- J301 pad 59: (no net) -> iMX8_LVDS0_A3_N
- J301 pad 6: (no net) -> Net-(J301-Pad6)
- J301 pad 60: (no net) -> Net-(J301-Pad60)
- J301 pad 61: (no net) -> Net-(J301-Pad61)
- J301 pad 62: (no net) -> Net-(J301-Pad62)
- J301 pad 63: (no net) -> Net-(J301-Pad63)
- J301 pad 65: (no net) -> Net-(J301-Pad65)
- J301 pad 66: (no net) -> Net-(J301-Pad66)
- J301 pad 67: (no net) -> Net-(J301-Pad67)
- J301 pad 68: (no net) -> Net-(J301-Pad68)
- J301 pad 69: (no net) -> Net-(J301-Pad69)
- J301 pad 70: (no net) -> Net-(J301-Pad70)
- J301 pad 72: (no net) -> Net-(J301-Pad72)
- J301 pad 73: (no net) -> Net-(J301-Pad73)
- J301 pad 74: (no net) -> Net-(J301-Pad74)
- J301 pad 75: (no net) -> iMX8_PWM1
- J301 pad 76: (no net) -> Net-(J301-Pad76)
- J301 pad 77: (no net) -> Net-(J301-Pad77)
- J301 pad 79: (no net) -> Net-(J301-Pad79)
- J301 pad 8: (no net) -> Net-(J301-Pad8)
- J301 pad 80: (no net) -> Net-(J301-Pad80)
- J301 pad 81: (no net) -> Net-(J301-Pad81)
- J301 pad 82: (no net) -> Net-(J301-Pad82)
- J301 pad 83: (no net) -> Net-(J301-Pad83)
- J301 pad 84: (no net) -> Net-(J301-Pad84)
- J301 pad 85: (no net) -> Net-(J301-Pad85)
- J301 pad 86: (no net) -> Net-(J301-Pad86)
- J301 pad 88: (no net) -> iMX8_GPIO2_IO17
- J301 pad 89: (no net) -> Net-(J301-Pad89)
- J301 pad 90: (no net) -> iMX8_GPIO2_IO18
- J301 pad 91: (no net) -> Net-(J301-Pad91)
- J301 pad 92: (no net) -> Net-(J301-Pad92)
- J301 pad 93: (no net) -> Net-(J301-Pad93)
- J301 pad 94: (no net) -> Net-(J301-Pad94)
- J301 pad 95: (no net) -> Net-(J301-Pad95)
- J301 pad 97: (no net) -> Net-(J301-Pad97)
- J301 pad 98: (no net) -> Net-(J301-Pad98)
- J301 pad 99: (no net) -> Net-(J301-Pad99)
- R10 pad 1: Net-(C13-Pad1) -> RESET
- R10 pad 2: +1V8 -> +3V3
- R11 pad 1: Net-(C14-Pad1) -> WAKE
- R11 pad 2: +1V8 -> +3V3
- R12 pad 1: Net-(C25-Pad1) -> +1V8
- R12 pad 2: +1V8 -> /PLL_AVDD
- R13 pad 2: Net-(J4-Pad6) -> Net-(J3-Pad6)
- R14 pad 1: Net-(J4-Pad4) -> Net-(J3-Pad4)
- R208 pad 1: FT813.GPIO3 -> GND
- R208 pad 2: +3V3 -> FT813.GPIO3
- R210 pad 2: FT813.GPIO1 -> FT813.GPIO0
- R211 pad 1: FT813.GPIO0 -> FT813.GPIO1
- R23 pad 2: /BL_PWM -> BL_PWM
- R301 pad 2: Net-(J6-Pad5) -> /exp/CTP_INT
- R302 pad 2: Net-(J6-Pad2) -> /exp/CTP_SDA
- R303 pad 2: Net-(J6-Pad1) -> /exp/CTP_SCL
- R304 pad 1: Net-(J6-Pad4) -> /exp/CTP_RST
- SW1 pad 2: Net-(C13-Pad1) -> RESET
- SW2 pad 1: Net-(C14-Pad1) -> WAKE
- SW201 pad 1: /periph/ESP32.PCM.SYNC -> Net-(C203-Pad1)
- U1 pad 12: (no net) -> Net-(U1-Pad12)
- U1 pad 23: (no net) -> Net-(U1-Pad23)
- U1 pad 24: (no net) -> Net-(U1-Pad24)
- U10 pad 1: (no net) -> Net-(U10-Pad1)
- U10 pad 15: (no net) -> Net-(U10-Pad15)
- U10 pad 2: (no net) -> Net-(U10-Pad2)
- U10 pad 3: (no net) -> Net-(U10-Pad3)
- U10 pad 4: (no net) -> Net-(U10-Pad4)
- U10 pad 5: (no net) -> Net-(U10-Pad5)
- U10 pad 6: (no net) -> Net-(U10-Pad6)
- U10 pad 7: (no net) -> Net-(U10-Pad7)
- U13 pad 1: Net-(RN1-Pad2) -> FT813_R1
- U13 pad 12: (no net) -> Net-(U13-Pad12)
- U13 pad 2: Net-(RN1-Pad1) -> FT813_R0
- U13 pad 23: /CTP_RST -> FT813_CTP_RST
- U13 pad 24: /CTP_INT -> FT813_CTP_INT
- U13 pad 25: /CTP_SCL -> FT813_CTP_SCL
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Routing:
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- added copper zone on PWR, net +1V8
- added copper zone on PWR, net +3V3
- added copper zone on PWR, net +VSYS
- added copper zone on B.Cu, net DISP_LED_A
- added copper zone on B.Cu, net DISP_LED_K
- added copper zone on GND, net GND
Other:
- copper layers 2 -> 4
- net class DISPLAY added: clearance 0.1524, trace_width 0.1524, via_dia 0.508, via_drill 0.254
- net class Default: clearance 0.18 -> 0.2; via_dia 0.6096 -> 0.6; via_drill 0.3048 -> 0.3
- net class FE310_L added: clearance 0.2, trace_width 0.2, via_dia 0.6, via_drill 0.3
- net class MODEM_USB added: clearance 0.1524, trace_width 0.1524, via_dia 0.508, via_drill 0.254
- rule trace_clearance: 0.18 -> 0.2
- rule via_min_drill: 0.3 -> 0.2

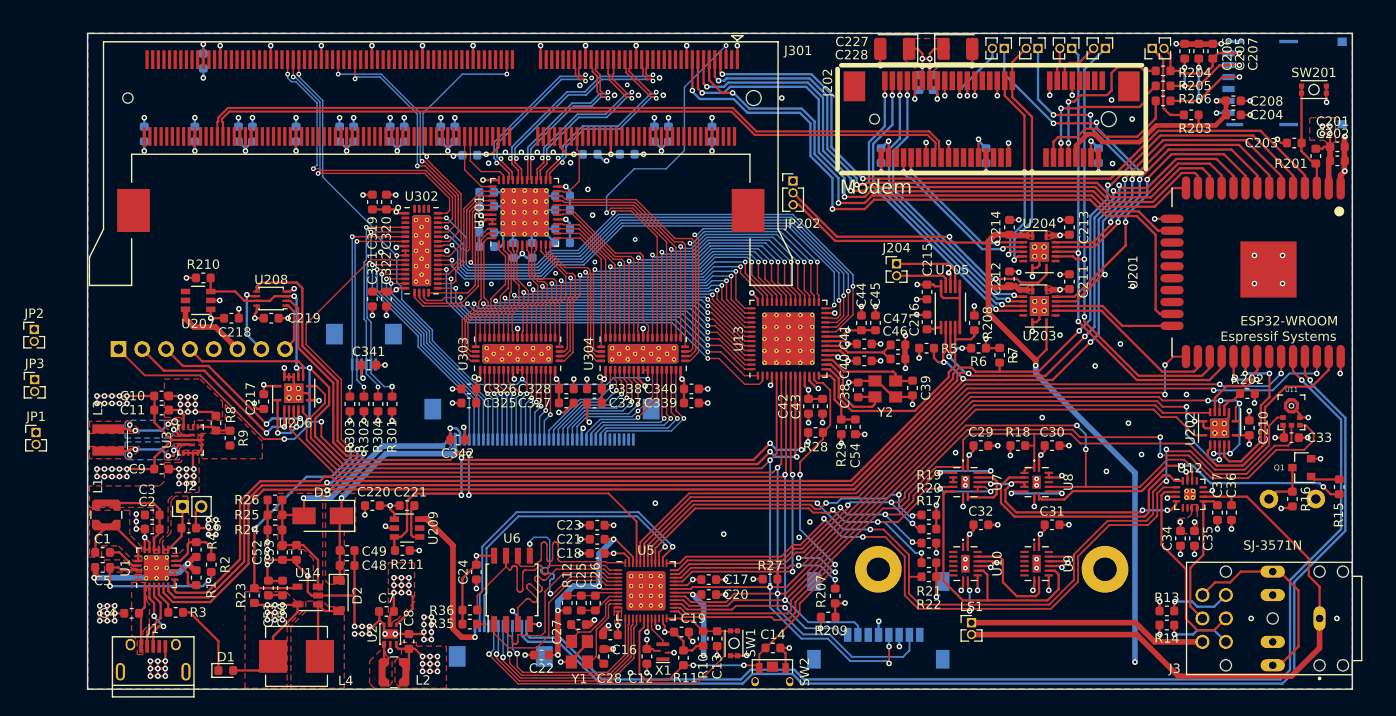
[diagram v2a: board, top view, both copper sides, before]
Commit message: display switch pull resistors added
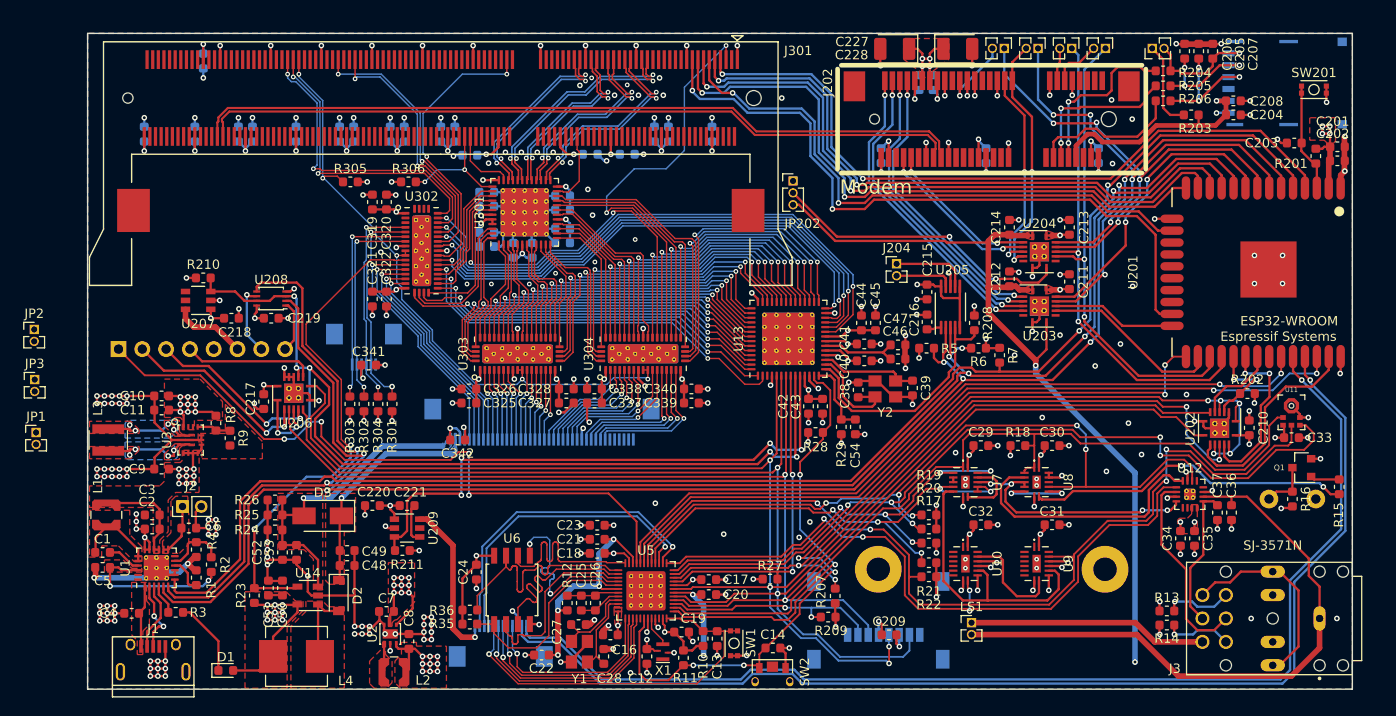
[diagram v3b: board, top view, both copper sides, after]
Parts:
- added C209: 0.1uF, Capacitor_SMD:C_0603_1608Metric, F.Cu at (182.8, 136.0)
- added R305: 47K, Resistor_SMD:R_0603_1608Metric, F.Cu at (125.2, 87.7)
- added R306: 100K, Resistor_SMD:R_0603_1608Metric, F.Cu at (131.4, 87.7)
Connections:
- J205 pad 1: SPI1.SS0 -> Net-(J205-Pad1)
- J205 pad 2: SPI1.MOSI -> SPI1.SS0
- J205 pad 3: Net-(J205-Pad3) -> SPI1.MOSI
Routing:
- net iMX8_GPIO2_IO18: track 7.26 -> 13.0 mm, vias 0 -> 2
- net +3V3: track 217.7 -> 220.3 mm, vias 84 -> 85
- net iMX8_GPIO3_IO13: track 66.1 -> 68.7 mm, vias 4 -> 5
- net SPI1.SS0: track 21.4 -> 23.9 mm
- net GND: track 417.5 -> 419.9 mm, vias 285 -> 286
- net SPI1.MOSI: track 157.6 -> 158.8 mm
